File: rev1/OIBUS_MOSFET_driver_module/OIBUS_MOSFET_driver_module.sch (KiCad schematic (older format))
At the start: 139 parts, among them J1 SWD, J10 +, J11 +, J12 +, J13 +, J2 UART, J3 5V - 24V, Molex Ultrafit, J4 +, J5 +, J6 +, J7 +, J8 +, J9 +, T1 DMG6402LVT, T10 DMG6402LVT, T2 DMG6402LVT, T3 DMG6402LVT, T4 DMG6402LVT, T5 DMG6402LVT, T6 DMG6402LVT, T7 DMG6402LVT, T8 DMG6402LVT, T9 DMG6402LVT, U1 TLP291, U10 STM32F303CCTx, U11 TLP291, U12 TLP291, U2 TLP291, U3 TLP291, U4 TLP291, U5 TLP291, U6 TLP291, U7 TLP291, U8 TLP291, U9 TCAN330, Y1 16M

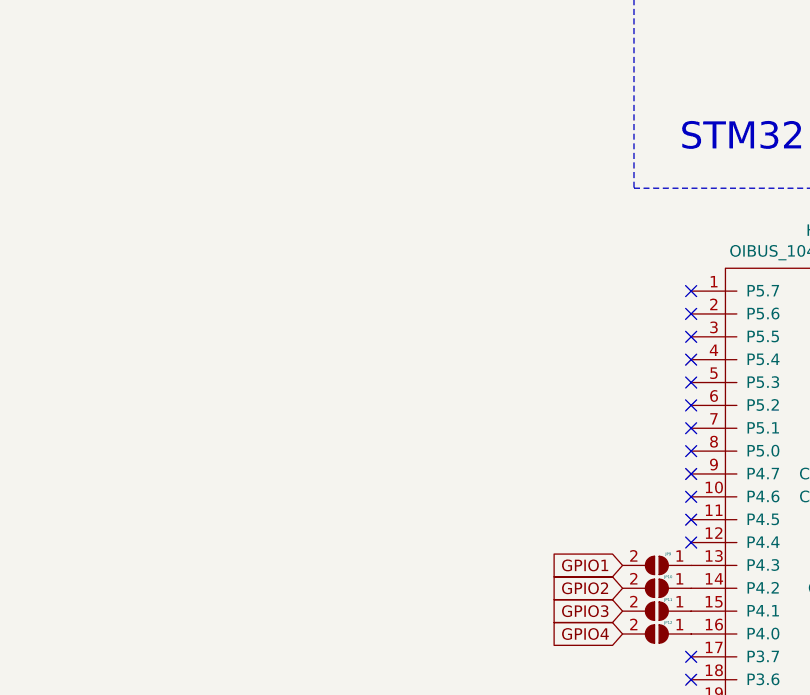
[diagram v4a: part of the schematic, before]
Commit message: removing vbus loop adding more 0ohms for connecting DGND to GND
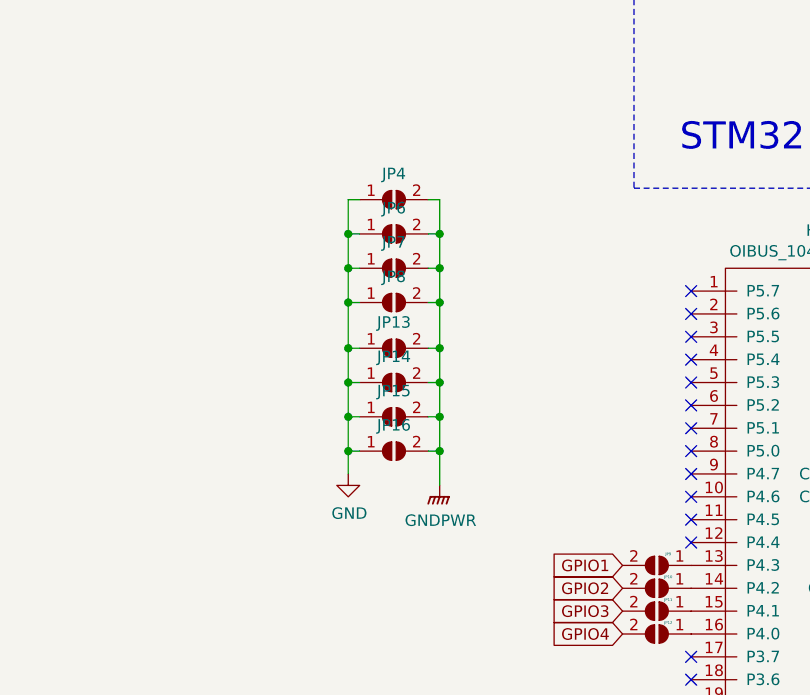
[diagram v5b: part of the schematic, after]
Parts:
- added JP13, JP14, JP15, JP16, JP4, JP6, JP7, JP8: 0 OHM, Resistors_SMD:R_0603, symbol Jumper:SolderJumper_2_Open
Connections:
- net GND: now also JP13.1 (A), JP14.1 (A), JP15.1 (A), JP16.1 (A), JP4.1 (A), JP6.1 (A), JP7.1 (A), JP8.1 (A)
- net GNDPWR: now also JP13.2 (B), JP14.2 (B), JP15.2 (B), JP16.2 (B), JP4.2 (B), JP6.2 (B), JP7.2 (B), JP8.2 (B)
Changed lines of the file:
@@
 NoConn ~ 14750 3300
 NoConn ~ 14750 3600
+$Comp
+L Jumper:SolderJumper_2_Open JP16
+U 1 1 5C18A8D8
+P 9200 6550
+F 0 "JP16" H 9200 6663 50  0000 C CNN
+F 1 "0 OHM" H 9200 6664 50  0001 C CNN
+F 2 "Resistors_SMD:R_0603" H 9200 6550 50  0001 C CNN
+F 3 "~" H 9200 6550 50  0001 C CNN
+	1    9200 6550
+	1    0    0    -1
+$EndComp
+$Comp
+L power:GND #PWR082
+U 1 1 5C18AEC6
+P 9000 6650
+F 0 "#PWR082" H 9000 6400 50  0001 C CNN
+F 1 "GND" H 9005 6477 50  0000 C CNN
+F 2 "" H 9000 6650 50  0001 C CNN
+F 3 "" H 9000 6650 50  0001 C CNN
+	1    9000 6650
+	1    0    0    -1
+$EndComp
+$Comp
+L power:GNDPWR #PWR083
+U 1 1 5C18B0D2
+P 9400 6700
+F 0 "#PWR083" H 9400 6500 50  0001 C CNN
+F 1 "GNDPWR" H 9404 6546 50  0000 C CNN
+F 2 "" H 9400 6650 50  0001 C CNN
+F 3 "" H 9400 6650 50  0001 C CNN
+	1    9400 6700
+	1    0    0    -1
+$EndComp
+Wire Wire Line
+	9400 6700 9400 6550
+Wire Wire Line
+	9400 6550 9350 6550
+Wire Wire Line
+	9050 6550 9000 6550
+Wire Wire Line
+	9000 6550 9000 6650
+$Comp
+L Jumper:SolderJumper_2_Open JP15
+U 1 1 5C35D503
+P 9200 6400
+F 0 "JP15" H 9200 6513 50  0000 C CNN
+F 1 "0 OHM" H 9200 6514 50  0001 C CNN
+F 2 "Resistors_SMD:R_0603" H 9200 6400 50  0001 C CNN
+F 3 "~" H 9200 6400 50  0001 C CNN
+	1    9200 6400
+	1    0    0    -1
+$EndComp
+$Comp
+L Jumper:SolderJumper_2_Open JP14
+U 1 1 5C35D62F
+P 9200 6250
+F 0 "JP14" H 9200 6363 50  0000 C CNN
+F 1 "0 OHM" H 9200 6364 50  0001 C CNN
+F 2 "Resistors_SMD:R_0603" H 9200 6250 50  0001 C CNN
+F 3 "~" H 9200 6250 50  0001 C CNN
+	1    9200 6250
+	1    0    0    -1
+$EndComp
+$Comp
+L Jumper:SolderJumper_2_Open JP13
+U 1 1 5C35D761
+P 9200 6100
+F 0 "JP13" H 9200 6213 50  0000 C CNN
+F 1 "0 OHM" H 9200 6214 50  0001 C CNN
+F 2 "Resistors_SMD:R_0603" H 9200 6100 50  0001 C CNN
+F 3 "~" H 9200 6100 50  0001 C CNN
+	1    9200 6100
+	1    0    0    -1
+$EndComp
+$Comp
+L Jumper:SolderJumper_2_Open JP8
+U 1 1 5C35D9AE
+P 9200 5900
+F 0 "JP8" H 9200 6013 50  0000 C CNN
+F 1 "0 OHM" H 9200 6014 50  0001 C CNN
+F 2 "Resistors_SMD:R_0603" H 9200 5900 50  0001 C CNN
+F 3 "~" H 9200 5900 50  0001 C CNN
+	1    9200 5900
+	1    0    0    -1
+$EndComp
+Wire Wire Line
+	9050 5900 9000 5900
+$Comp
+L Jumper:SolderJumper_2_Open JP7
+U 1 1 5C35D9B7
+P 9200 5750
+F 0 "JP7" H 9200 5863 50  0000 C CNN
+F 1 "0 OHM" H 9200 5864 50  0001 C CNN
+F 2 "Resistors_SMD:R_0603" H 9200 5750 50  0001 C CNN
+F 3 "~" H 9200 5750 50  0001 C CNN
+	1    9200 5750
+	1    0    0    -1
+$EndComp
+$Comp
+L Jumper:SolderJumper_2_Open JP6
+U 1 1 5C35D9BE
+P 9200 5600
+F 0 "JP6" H 9200 5713 50  0000 C CNN
+F 1 "0 OHM" H 9200 5714 50  0001 C CNN
+F 2 "Resistors_SMD:R_0603" H 9200 5600 50  0001 C CNN
+F 3 "~" H 9200 5600 50  0001 C CNN
+	1    9200 5600
+	1    0    0    -1
+$EndComp
+$Comp
+L Jumper:SolderJumper_2_Open JP4
+U 1 1 5C35D9C5
+P 9200 5450
+F 0 "JP4" H 9200 5563 50  0000 C CNN
+F 1 "0 OHM" H 9200 5564 50  0001 C CNN
+F 2 "Resistors_SMD:R_0603" H 9200 5450 50  0001 C CNN
+F 3 "~" H 9200 5450 50  0001 C CNN
+	1    9200 5450
+	1    0    0    -1
+$EndComp
+Wire Wire Line
+	9000 5900 9000 6100
+Connection ~ 9000 6550
+Wire Wire Line
+	9050 6400 9000 6400
+Connection ~ 9000 6400
+Wire Wire Line
+	9000 6400 9000 6550
+Wire Wire Line
+	9050 6250 9000 6250
+Connection ~ 9000 6250
+Wire Wire Line
+	9000 6250 9000 6400
+Wire Wire Line
+	9050 6100 9000 6100
+Connection ~ 9000 6100
+Wire Wire Line
+	9000 6100 9000 6250
+Connection ~ 9000 5900
+Wire Wire Line
+	9050 5600 9000 5600
+Wire Wire Line
+	9050 5450 9000 5450
+Wire Wire Line
+	9000 5450 9000 5600
+Connection ~ 9000 5600
+Wire Wire Line
+	9400 6550 9400 6400
+Wire Wire Line
+	9400 5450 9350 5450
+Connection ~ 9400 6550
+Wire Wire Line
+	9350 5600 9400 5600
+Connection ~ 9400 5600
+Wire Wire Line
+	9400 5600 9400 5450
+Wire Wire Line
+	9350 5900 9400 5900
+Connection ~ 9400 5900
+Wire Wire Line
+	9350 6100 9400 6100
+Connection ~ 9400 6100
+Wire Wire Line
+	9400 6100 9400 5900
+Wire Wire Line
+	9350 6250 9400 6250
+Connection ~ 9400 6250
+Wire Wire Line
+	9400 6250 9400 6100
+Wire Wire Line
+	9350 6400 9400 6400
+Connection ~ 9400 6400
+Wire Wire Line
+	9400 6400 9400 6250
+Wire Wire Line
+	9400 5600 9400 5750
+Wire Wire Line
+	9000 5600 9000 5750
+Wire Wire Line
+	9350 5750 9400 5750
+Connection ~ 9400 5750
+Wire Wire Line
+	9400 5750 9400 5900
+Wire Wire Line
+	9050 5750 9000 5750
+Connection ~ 9000 5750
+Wire Wire Line
+	9000 5750 9000 5900
 $EndSCHEMATC

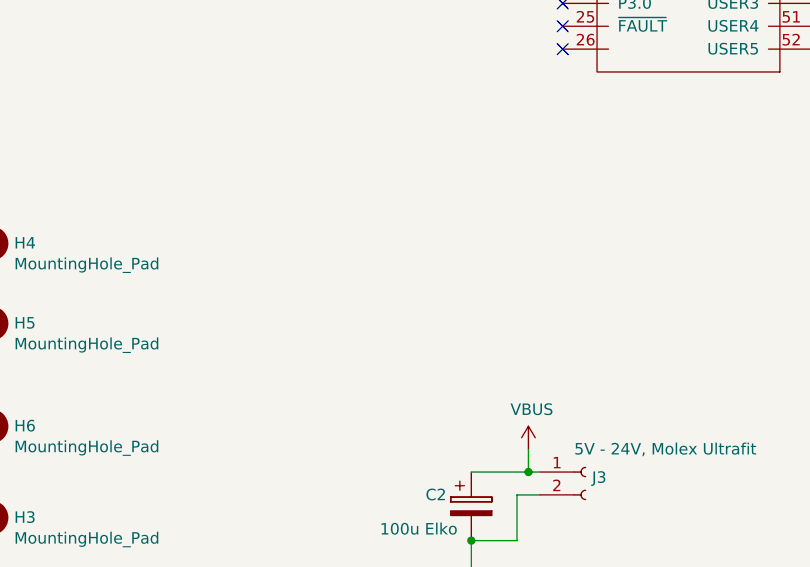
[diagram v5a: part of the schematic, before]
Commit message: adding more jumpers, removing newer kicad footprint paths from project into global, adding fiducials
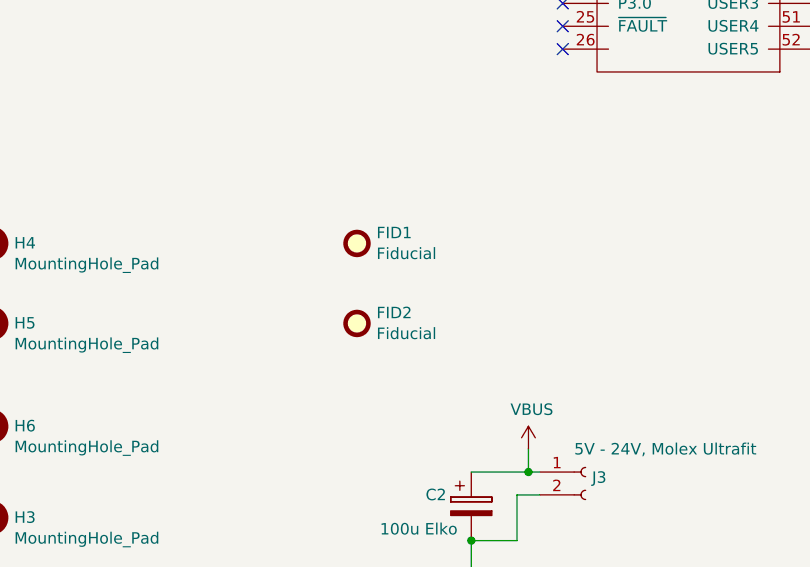
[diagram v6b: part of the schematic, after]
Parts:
- added FID1, FID2: Fiducial, Fiducial:Fiducial_1mm_Dia_2mm_Outer, symbol Mechanical:Fiducial
- JP10, JP11, JP12, JP13, JP14, JP15, JP16, JP21, JP22, JP23, JP24, JP25, JP26, JP27, JP28, JP29, JP4, JP5, JP6, JP7, JP8, JP9: footprint Resistors_SMD:R_0603 -> Resistor_SMD:R_0603_1608Metric
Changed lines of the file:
@@
 F 0 "JP21" H 14950 6563 50  0000 C CNN
 F 1 "0 OHM" H 14950 6564 50  0001 C CNN
-F 2 "Resistors_SMD:R_0603" H 14950 6450 50  0001 C CNN
+F 2 "Resistor_SMD:R_0603_1608Metric" H 14950 6450 50  0001 C CNN
 F 3 "~" H 14950 6450 50  0001 C CNN
 	1    14950 6450
@@
 F 0 "JP22" H 14950 6750 50  0000 C CNN
 F 1 "0 OHM" H 14950 6550 50  0001 C CNN
-F 2 "Resistors_SMD:R_0603" H 14950 6650 50  0001 C CNN
+F 2 "Resistor_SMD:R_0603_1608Metric" H 14950 6650 50  0001 C CNN
 F 3 "~" H 14950 6650 50  0001 C CNN
 	1    14950 6650
@@
 F 0 "JP23" H 14950 6950 50  0000 C CNN
 F 1 "0 OHM" H 14950 6750 50  0001 C CNN
-F 2 "Resistors_SMD:R_0603" H 14950 6850 50  0001 C CNN
+F 2 "Resistor_SMD:R_0603_1608Metric" H 14950 6850 50  0001 C CNN
 F 3 "~" H 14950 6850 50  0001 C CNN
 	1    14950 6850
@@
 F 0 "JP24" H 14950 7150 50  0000 C CNN
 F 1 "0 OHM" H 14950 6950 50  0001 C CNN
-F 2 "Resistors_SMD:R_0603" H 14950 7050 50  0001 C CNN
+F 2 "Resistor_SMD:R_0603_1608Metric" H 14950 7050 50  0001 C CNN
 F 3 "~" H 14950 7050 50  0001 C CNN
 	1    14950 7050
@@
 F 0 "JP25" H 14950 7350 50  0000 C CNN
 F 1 "0 OHM" H 14950 7150 50  0001 C CNN
-F 2 "Resistors_SMD:R_0603" H 14950 7250 50  0001 C CNN
+F 2 "Resistor_SMD:R_0603_1608Metric" H 14950 7250 50  0001 C CNN
 F 3 "~" H 14950 7250 50  0001 C CNN
 	1    14950 7250
@@
 F 0 "JP26" H 14950 7550 50  0000 C CNN
 F 1 "0 OHM" H 14950 7350 50  0001 C CNN
-F 2 "Resistors_SMD:R_0603" H 14950 7450 50  0001 C CNN
+F 2 "Resistor_SMD:R_0603_1608Metric" H 14950 7450 50  0001 C CNN
 F 3 "~" H 14950 7450 50  0001 C CNN
 	1    14950 7450
@@
 F 0 "JP29" H 13250 8450 50  0000 C CNN
 F 1 "0 OHM" H 13250 8250 50  0000 C CNN
-F 2 "Resistors_SMD:R_0603" H 13250 8350 50  0001 C CNN
+F 2 "Resistor_SMD:R_0603_1608Metric" H 13250 8350 50  0001 C CNN
 F 3 "~" H 13250 8350 50  0001 C CNN
 	1    13250 8350
@@
 F 0 "JP27" H 14950 7750 50  0000 C CNN
 F 1 "0 OHM" H 14950 7550 50  0001 C CNN
-F 2 "Resistors_SMD:R_0603" H 14950 7650 50  0001 C CNN
+F 2 "Resistor_SMD:R_0603_1608Metric" H 14950 7650 50  0001 C CNN
 F 3 "~" H 14950 7650 50  0001 C CNN
 	1    14950 7650
@@
 F 0 "JP28" H 14950 6163 50  0000 C CNN
 F 1 "0 OHM" H 14950 6164 50  0001 C CNN
-F 2 "Resistors_SMD:R_0603" H 14950 6050 50  0001 C CNN
+F 2 "Resistor_SMD:R_0603_1608Metric" H 14950 6050 50  0001 C CNN
 F 3 "~" H 14950 6050 50  0001 C CNN
 	1    14950 6050
@@
 F 0 "JP5" H 11700 8000 12  0000 C CNN
 F 1 "SolderJumper_2_Open" H 11750 8164 50  0001 C CNN
-F 2 "Resistors_SMD:R_0603" H 11750 8050 50  0001 C CNN
+F 2 "Resistor_SMD:R_0603_1608Metric" H 11750 8050 50  0001 C CNN
 F 3 "~" H 11750 8050 50  0001 C CNN
 	1    11750 8050
@@
 F 0 "JP10" H 10300 7100 12  0000 C CNN
 F 1 "SolderJumper_2_Open" H 10350 7264 50  0001 C CNN
-F 2 "Resistors_SMD:R_0603" H 10350 7150 50  0001 C CNN
+F 2 "Resistor_SMD:R_0603_1608Metric" H 10350 7150 50  0001 C CNN
 F 3 "~" H 10350 7150 50  0001 C CNN
 	1    10350 7150
@@
 F 0 "JP9" H 10300 7000 12  0000 C CNN
 F 1 "SolderJumper_2_Open" H 10350 7164 50  0001 C CNN
-F 2 "Resistors_SMD:R_0603" H 10350 7050 50  0001 C CNN
+F 2 "Resistor_SMD:R_0603_1608Metric" H 10350 7050 50  0001 C CNN
 F 3 "~" H 10350 7050 50  0001 C CNN
 	1    10350 7050
@@
 F 0 "JP12" H 10300 7300 12  0000 C CNN
 F 1 "SolderJumper_2_Open" H 10350 7464 50  0001 C CNN
-F 2 "Resistors_SMD:R_0603" H 10350 7350 50  0001 C CNN
+F 2 "Resistor_SMD:R_0603_1608Metric" H 10350 7350 50  0001 C CNN
 F 3 "~" H 10350 7350 50  0001 C CNN
 	1    10350 7350
@@
 F 0 "JP11" H 10300 7200 12  0000 C CNN
 F 1 "SolderJumper_2_Open" H 10350 7364 50  0001 C CNN
-F 2 "Resistors_SMD:R_0603" H 10350 7250 50  0001 C CNN
+F 2 "Resistor_SMD:R_0603_1608Metric" H 10350 7250 50  0001 C CNN
 F 3 "~" H 10350 7250 50  0001 C CNN
 	1    10350 7250
@@
 F 0 "JP16" H 9200 6663 50  0000 C CNN
 F 1 "0 OHM" H 9200 6664 50  0001 C CNN
-F 2 "Resistors_SMD:R_0603" H 9200 6550 50  0001 C CNN
+F 2 "Resistor_SMD:R_0603_1608Metric" H 9200 6550 50  0001 C CNN
 F 3 "~" H 9200 6550 50  0001 C CNN
 	1    9200 6550
@@
 F 0 "JP15" H 9200 6513 50  0000 C CNN
 F 1 "0 OHM" H 9200 6514 50  0001 C CNN
-F 2 "Resistors_SMD:R_0603" H 9200 6400 50  0001 C CNN
+F 2 "Resistor_SMD:R_0603_1608Metric" H 9200 6400 50  0001 C CNN
 F 3 "~" H 9200 6400 50  0001 C CNN
 	1    9200 6400
@@
 F 0 "JP14" H 9200 6363 50  0000 C CNN
 F 1 "0 OHM" H 9200 6364 50  0001 C CNN
-F 2 "Resistors_SMD:R_0603" H 9200 6250 50  0001 C CNN
+F 2 "Resistor_SMD:R_0603_1608Metric" H 9200 6250 50  0001 C CNN
 F 3 "~" H 9200 6250 50  0001 C CNN
 	1    9200 6250
@@
 F 0 "JP13" H 9200 6213 50  0000 C CNN
 F 1 "0 OHM" H 9200 6214 50  0001 C CNN
-F 2 "Resistors_SMD:R_0603" H 9200 6100 50  0001 C CNN
+F 2 "Resistor_SMD:R_0603_1608Metric" H 9200 6100 50  0001 C CNN
 F 3 "~" H 9200 6100 50  0001 C CNN
 	1    9200 6100
@@
 F 0 "JP8" H 9200 6013 50  0000 C CNN
 F 1 "0 OHM" H 9200 6014 50  0001 C CNN
-F 2 "Resistors_SMD:R_0603" H 9200 5900 50  0001 C CNN
+F 2 "Resistor_SMD:R_0603_1608Metric" H 9200 5900 50  0001 C CNN
 F 3 "~" H 9200 5900 50  0001 C CNN
 	1    9200 5900
@@
 F 0 "JP7" H 9200 5863 50  0000 C CNN
 F 1 "0 OHM" H 9200 5864 50  0001 C CNN
-F 2 "Resistors_SMD:R_0603" H 9200 5750 50  0001 C CNN
+F 2 "Resistor_SMD:R_0603_1608Metric" H 9200 5750 50  0001 C CNN
 F 3 "~" H 9200 5750 50  0001 C CNN
 	1    9200 5750
@@
 F 0 "JP6" H 9200 5713 50  0000 C CNN
 F 1 "0 OHM" H 9200 5714 50  0001 C CNN
-F 2 "Resistors_SMD:R_0603" H 9200 5600 50  0001 C CNN
+F 2 "Resistor_SMD:R_0603_1608Metric" H 9200 5600 50  0001 C CNN
 F 3 "~" H 9200 5600 50  0001 C CNN
 	1    9200 5600
@@
 F 0 "JP4" H 9200 5563 50  0000 C CNN
 F 1 "0 OHM" H 9200 5564 50  0001 C CNN
-F 2 "Resistors_SMD:R_0603" H 9200 5450 50  0001 C CNN
+F 2 "Resistor_SMD:R_0603_1608Metric" H 9200 5450 50  0001 C CNN
 F 3 "~" H 9200 5450 50  0001 C CNN
 	1    9200 5450
@@
 Wire Wire Line
 	9000 5750 9000 5900
+$Comp
+L Mechanical:Fiducial FID1
+U 1 1 5C1E4BDC
+P 9600 9200
+F 0 "FID1" H 9685 9246 50  0000 L CNN
+F 1 "Fiducial" H 9685 9155 50  0000 L CNN
+F 2 "Fiducial:Fiducial_1mm_Dia_2mm_Outer" H 9600 9200 50  0001 C CNN
+F 3 "~" H 9600 9200 50  0001 C CNN
+	1    9600 9200
+	1    0    0    -1
+$EndComp
+$Comp
+L Mechanical:Fiducial FID2
+U 1 1 5C1E5264
+P 9600 9550
+F 0 "FID2" H 9685 9596 50  0000 L CNN
+F 1 "Fiducial" H 9685 9505 50  0000 L CNN
+F 2 "Fiducial:Fiducial_1mm_Dia_2mm_Outer" H 9600 9550 50  0001 C CNN
+F 3 "~" H 9600 9550 50  0001 C CNN
+	1    9600 9550
+	1    0    0    -1
+$EndComp
 $EndSCHEMATC

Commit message: adding finishing touches
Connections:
- net Rx: now also JP2.2 (C); no longer JP2.3 (B)
- net Tx: now also JP1.2 (C); no longer JP1.3 (B)
- net at J2.2 (Pin_2): now also JP1.3 (B); no longer JP1.2 (C)
- net at J2.1 (Pin_1): now also JP2.3 (B); no longer JP2.2 (C)
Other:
- moved on the sheet: JP2
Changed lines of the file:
@@
 encoding utf-8
 Sheet 1 1
-Title "OIBUS MOSFET Driver Module (P4L3)(P5)(V)(USER)(COMM)"
+Title "OIBUS MOSFET Driver Module (P4L4)(V*)(USER02)(COMM)"
 Date "2018-12-05"
 Rev "1"
@@
 Wire Wire Line
 	10850 1050 11750 1050
-Text GLabel 12200 6950 2    50   Input ~ 0
+Text GLabel 12150 7100 2    50   Input ~ 0
 Tx
-Text GLabel 12100 7150 2    50   Input ~ 0
+Text GLabel 12150 7350 2    50   Input ~ 0
 Rx
 $Comp
 L Jumper:SolderJumper_3_Open JP2
 U 1 1 5E09018A
-P 11850 7150
-F 0 "JP2" H 12000 7000 50  0000 C CNN
-F 1 "SolderJumper_3_Open" H 11850 7353 50  0001 C CNN
-F 2 "Jumper:SolderJumper-3_P1.3mm_Open_RoundedPad1.0x1.5mm" H 11850 7150 50  0001 C CNN
-F 3 "~" H 11850 7150 50  0001 C CNN
-	1    11850 7150
+P 11850 7200
+F 0 "JP2" H 12000 7050 50  0000 C CNN
+F 1 "SolderJumper_3_Open" H 11850 7403 50  0001 C CNN
+F 2 "Jumper:SolderJumper-3_P1.3mm_Open_RoundedPad1.0x1.5mm" H 11850 7200 50  0001 C CNN
+F 3 "~" H 11850 7200 50  0001 C CNN
+	1    11850 7200
 	1    0    0    -1
 $EndComp
@@
 	11750 7500 11800 7500
 Wire Wire Line
-	12100 7150 12050 7150
-Wire Wire Line
 	11650 7150 11600 7150
 $Comp
@@
 	-1   0    0    1
 $EndComp
-Wire Wire Line
-	12400 7150 12400 7400
-Wire Wire Line
-	12400 7400 11850 7400
-Wire Wire Line
-	11850 7400 11850 7300
 Text GLabel 13350 3500 0    50   Input ~ 0
 GPIO1
@@
 Wire Wire Line
 	11600 7050 11750 7050
-Wire Wire Line
-	12400 7050 12100 7050
-Wire Wire Line
-	12100 7050 12100 7100
-Wire Wire Line
-	12100 7100 12000 7100
 NoConn ~ 14750 3300
 NoConn ~ 14750 3600
@@
 	1    0    0    -1
 $EndComp
+Wire Wire Line
+	12400 7050 12350 7050
+Wire Wire Line
+	12350 7050 12350 6950
+Wire Wire Line
+	12350 6950 12200 6950
+Wire Wire Line
+	11850 7350 12150 7350
+Wire Wire Line
+	12400 7150 12350 7150
+Wire Wire Line
+	12350 7150 12350 7200
+Wire Wire Line
+	12350 7200 12050 7200
+Wire Wire Line
+	12150 7100 12000 7100
+Wire Wire Line
+	11650 7150 11650 7200
 $EndSCHEMATC

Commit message: fixed wrong optocoupler footprint
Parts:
- U1, U11, U12, U2, U3, U4, U5, U6, U7, U8: footprint Package_DIP:SMDIP-4_W7.62mm -> TLP291(SE:SOIC127P700X220-4N
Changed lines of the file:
@@
 F 0 "U1" H 2600 2875 50  0000 C CNN
 F 1 "TLP291" H 2600 2784 50  0000 C CNN
-F 2 "Package_DIP:SMDIP-4_W7.62mm" H 2400 2350 50  0001 L CIN
+F 2 "TLP291(SE:SOIC127P700X220-4N" H 2400 2350 50  0001 L CIN
 F 3 "https://toshiba.semicon-storage.com/info/docget.jsp?did=12884&prodName=TLP291" H 2600 2550 50  0001 L CNN
 	1    2600 2550
@@
 F 0 "U2" H 2600 3825 50  0000 C CNN
 F 1 "TLP291" H 2600 3734 50  0000 C CNN
-F 2 "Package_DIP:SMDIP-4_W7.62mm" H 2400 3300 50  0001 L CIN
+F 2 "TLP291(SE:SOIC127P700X220-4N" H 2400 3300 50  0001 L CIN
 F 3 "https://toshiba.semicon-storage.com/info/docget.jsp?did=12884&prodName=TLP291" H 2600 3500 50  0001 L CNN
 	1    2600 3500
@@
 F 0 "U3" H 2600 4725 50  0000 C CNN
 F 1 "TLP291" H 2600 4634 50  0000 C CNN
-F 2 "Package_DIP:SMDIP-4_W7.62mm" H 2400 4200 50  0001 L CIN
+F 2 "TLP291(SE:SOIC127P700X220-4N" H 2400 4200 50  0001 L CIN
 F 3 "https://toshiba.semicon-storage.com/info/docget.jsp?did=12884&prodName=TLP291" H 2600 4400 50  0001 L CNN
 	1    2600 4400
@@
 F 0 "U4" H 2600 5575 50  0000 C CNN
 F 1 "TLP291" H 2600 5484 50  0000 C CNN
-F 2 "Package_DIP:SMDIP-4_W7.62mm" H 2400 5050 50  0001 L CIN
+F 2 "TLP291(SE:SOIC127P700X220-4N" H 2400 5050 50  0001 L CIN
 F 3 "https://toshiba.semicon-storage.com/info/docget.jsp?did=12884&prodName=TLP291" H 2600 5250 50  0001 L CNN
 	1    2600 5250
@@
 F 0 "U5" H 2600 6375 50  0000 C CNN
 F 1 "TLP291" H 2600 6284 50  0000 C CNN
-F 2 "Package_DIP:SMDIP-4_W7.62mm" H 2400 5850 50  0001 L CIN
+F 2 "TLP291(SE:SOIC127P700X220-4N" H 2400 5850 50  0001 L CIN
 F 3 "https://toshiba.semicon-storage.com/info/docget.jsp?did=12884&prodName=TLP291" H 2600 6050 50  0001 L CNN
 	1    2600 6050
@@
 F 0 "U6" H 2600 7225 50  0000 C CNN
 F 1 "TLP291" H 2600 7134 50  0000 C CNN
-F 2 "Package_DIP:SMDIP-4_W7.62mm" H 2400 6700 50  0001 L CIN
+F 2 "TLP291(SE:SOIC127P700X220-4N" H 2400 6700 50  0001 L CIN
 F 3 "https://toshiba.semicon-storage.com/info/docget.jsp?did=12884&prodName=TLP291" H 2600 6900 50  0001 L CNN
 	1    2600 6900
@@
 F 0 "U7" H 2600 7975 50  0000 C CNN
 F 1 "TLP291" H 2600 7884 50  0000 C CNN
-F 2 "Package_DIP:SMDIP-4_W7.62mm" H 2400 7450 50  0001 L CIN
+F 2 "TLP291(SE:SOIC127P700X220-4N" H 2400 7450 50  0001 L CIN
 F 3 "https://toshiba.semicon-storage.com/info/docget.jsp?did=12884&prodName=TLP291" H 2600 7650 50  0001 L CNN
 	1    2600 7650
@@
 F 0 "U8" H 2600 8825 50  0000 C CNN
 F 1 "TLP291" H 2600 8734 50  0000 C CNN
-F 2 "Package_DIP:SMDIP-4_W7.62mm" H 2400 8300 50  0001 L CIN
+F 2 "TLP291(SE:SOIC127P700X220-4N" H 2400 8300 50  0001 L CIN
 F 3 "https://toshiba.semicon-storage.com/info/docget.jsp?did=12884&prodName=TLP291" H 2600 8500 50  0001 L CNN
 	1    2600 8500
@@
 F 0 "U11" H 2600 9575 50  0000 C CNN
 F 1 "TLP291" H 2600 9484 50  0000 C CNN
-F 2 "Package_DIP:SMDIP-4_W7.62mm" H 2400 9050 50  0001 L CIN
+F 2 "TLP291(SE:SOIC127P700X220-4N" H 2400 9050 50  0001 L CIN
 F 3 "https://toshiba.semicon-storage.com/info/docget.jsp?did=12884&prodName=TLP291" H 2600 9250 50  0001 L CNN
 	1    2600 9250
@@
 F 0 "U12" H 2600 10425 50  0000 C CNN
 F 1 "TLP291" H 2600 10334 50  0000 C CNN
-F 2 "Package_DIP:SMDIP-4_W7.62mm" H 2400 9900 50  0001 L CIN
+F 2 "TLP291(SE:SOIC127P700X220-4N" H 2400 9900 50  0001 L CIN
 F 3 "https://toshiba.semicon-storage.com/info/docget.jsp?did=12884&prodName=TLP291" H 2600 10100 50  0001 L CNN
 	1    2600 10100
